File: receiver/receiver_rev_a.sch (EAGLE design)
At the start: 1 part

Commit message: Mostly done with the receiver
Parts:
- added C1, C2, C3: 100uF, microbuilder:CAP_CERAMIC1206
- added C4: 0.1uF, microbuilder:CAP_CERAMIC0603MINI
- added CN1: (no value), microbuilder:DCBARRELPTH
- added FID1, FID2, FID3, FID4, FID5, FID6: FIDUCIAL, adafruit:FIDUCIAL
- added FUSE: (no value), Custom:MINI-FUSE-HOLDER3557
- added J1: POWERPOLE_POWER45A_HORIZONTAL_DRILL, powerpoles:POWERPOLE_POWER45A_HORIZONTAL_DRILL
- added JP1: (no value), SparkFun-Connectors:M04PTH
- added JP2: (no value), SparkFun-Connectors:M02PTH4
- added OUT1, OUT2, OUT3: MC4, con-phoenix-381_l:MC4
- added Q1, Q2, Q3: (no value), Custom:DMN1019USN
- added R1, R10, R2, R3, R4, R5, R6, R7, R8, R9: 120, microbuilder:RESISTOR0603MINI
- added R11, R12: 220, microbuilder:RESISTOR0603MINI
- added R13, R14, R15: 10k, microbuilder:RESISTOR0603MINI
- added SWITCH: (no value), Custom:DIP-SWITCH-3PIN194
- added U$3, U$4, U$5, U$6: MOUNTINGHOLE2.5, microbuilder:MOUNTINGHOLE2.5
- added U$7: (no value), Custom:RJHSE-5381
- added U1: (no value), maxim:MAX3093/94UE
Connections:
- new net A+: R1.2, U$7.1, U1.A+
- new net A-: R1.1, U$7.2, U1.A-
- new net B+: R2.2, U$7.3, U1.B+
- new net B-: R2.1, U$7.6, U1.B-
- new net C+: R3.2, U$7.4, U1.C+
- new net C-: R3.1, U$7.5, U1.C-
- new net CLOCK: JP1.1, R6.2, R7.2, R9.2, U1.YD
- new net D+: R4.2, U$7.7, U1.D+
- new net D-: R4.1, U$7.8, U1.D-
- new net DATA1: JP1.4, R5.2, U1.YA
- new net DATA2: JP1.3, R8.2, U1.YB
- new net DATA3: JP1.2, R10.2, U1.YC
- new net GATE1: Q1.G, R13.1, SWITCH.1B
- new net GATE2: Q2.G, R14.1, SWITCH.2B
- new net GATE3: Q3.G, R15.1, SWITCH.3B
- new net GND: C4.P$2, CN1.GND, J1.GND, JP2.2, Q1.S, Q2.S, Q3.S, R11.1, R12.1, R13.2, R14.2, R15.2, U$7.SH, U1.GND
- new net N$1: OUT1.2.SK, R5.1
- new net N$10: R11.2, U$7.GC
- new net N$11: R12.2, U$7.YC
- new net N$2: OUT1.3.SK, R6.1
- new net N$3: C1.P$2, OUT1.4.SK, Q1.D
- new net N$4: OUT2.2.SK, R8.1
- new net N$5: OUT2.3.SK, R7.1
- new net N$6: C2.P$2, OUT2.4.SK, Q2.D
- new net N$7: OUT3.2.SK, R10.1
- new net N$8: OUT3.3.SK, R9.1
- new net N$9: C3.P$2, OUT3.4.SK, Q3.D
- new net PREFUSE_VCC: CN1.PWR, FUSE.1, J1.V+, JP2.1, U$7.YA
- new net VCC: C1.P$1, C2.P$1, C3.P$1, C4.P$1, FUSE.2, OUT1.1.SK, OUT2.1.SK, OUT3.1.SK, SWITCH.1A, SWITCH.2A, SWITCH.3A, U$7.GA, U1.ENAC, U1.ENBD, U1.VCC

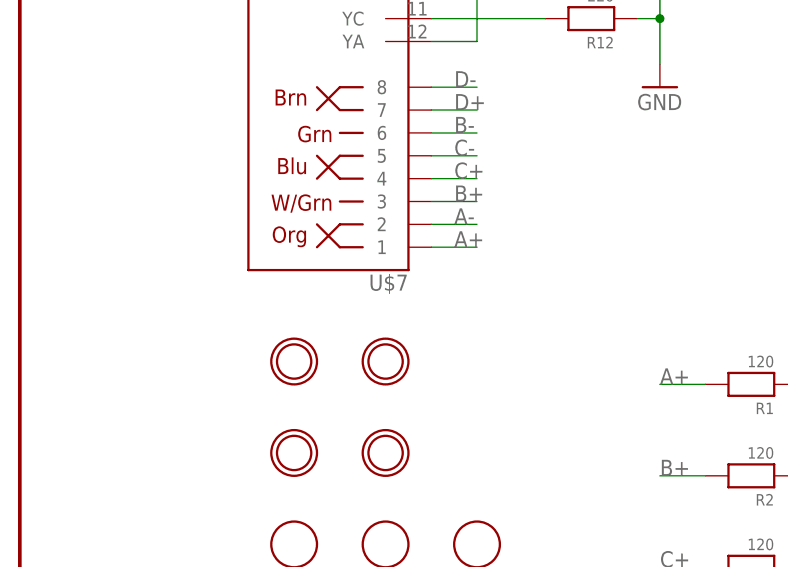
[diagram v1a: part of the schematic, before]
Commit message: Almost done with cape routing
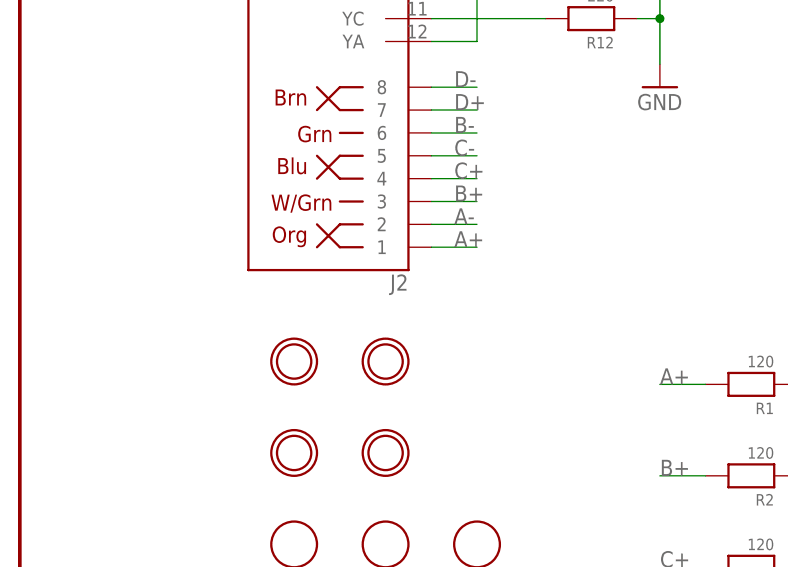
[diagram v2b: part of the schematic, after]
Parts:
- renumbered U$7 to J2
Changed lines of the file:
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@@
 <part name="U$5" library="microbuilder" deviceset="MOUNTINGHOLE" device="2.5"/>
 <part name="U$6" library="microbuilder" deviceset="MOUNTINGHOLE" device="2.5"/>
-<part name="U$7" library="Custom" deviceset="RJHSE-5381" device=""/>
+<part name="J2" library="Custom" deviceset="RJHSE-5381" device=""/>
 <part name="Q1" library="Custom" deviceset="DMN1019USN" device=""/>
 <part name="FUSE" library="Custom" deviceset="MINI-FUSE-HOLDER" device="3557"/>
@@
 <instance part="U$5" gate="G$1" x="40.64" y="58.42"/>
 <instance part="U$6" gate="G$1" x="30.48" y="48.26"/>
-<instance part="U$7" gate="G$1" x="33.02" y="81.28" rot="R180"/>
+<instance part="J2" gate="G$1" x="33.02" y="81.28" rot="R180"/>
 <instance part="Q1" gate="G$1" x="198.12" y="149.86"/>
 <instance part="FUSE" gate="G$1" x="63.5" y="154.94"/>
@@
 <net name="A+" class="0">
 <segment>
-<pinref part="U$7" gate="G$1" pin="1"/>
+<pinref part="J2" gate="G$1" pin="1"/>
 <wire x1="45.72" y1="71.12" x2="50.8" y2="71.12" width="0.1524" layer="91"/>
 <label x="48.26" y="71.12" size="1.778" layer="95"/>
@@
 <net name="A-" class="0">
 <segment>
-<pinref part="U$7" gate="G$1" pin="2"/>
+<pinref part="J2" gate="G$1" pin="2"/>
 <wire x1="45.72" y1="73.66" x2="50.8" y2="73.66" width="0.1524" layer="91"/>
 <label x="48.26" y="73.66" size="1.778" layer="95"/>
@@
 <net name="B+" class="0">
 <segment>
-<pinref part="U$7" gate="G$1" pin="3"/>
+<pinref part="J2" gate="G$1" pin="3"/>
 <wire x1="45.72" y1="76.2" x2="50.8" y2="76.2" width="0.1524" layer="91"/>
 <label x="48.26" y="76.2" size="1.778" layer="95"/>
@@
 <net name="C+" class="0">
 <segment>
-<pinref part="U$7" gate="G$1" pin="4"/>
+<pinref part="J2" gate="G$1" pin="4"/>
 <wire x1="45.72" y1="78.74" x2="50.8" y2="78.74" width="0.1524" layer="91"/>
 <label x="48.26" y="78.74" size="1.778" layer="95"/>
@@
 <net name="C-" class="0">
 <segment>
-<pinref part="U$7" gate="G$1" pin="5"/>
+<pinref part="J2" gate="G$1" pin="5"/>
 <wire x1="45.72" y1="81.28" x2="50.8" y2="81.28" width="0.1524" layer="91"/>
 <label x="48.26" y="81.28" size="1.778" layer="95"/>
@@
 <net name="B-" class="0">
 <segment>
-<pinref part="U$7" gate="G$1" pin="6"/>
+<pinref part="J2" gate="G$1" pin="6"/>
 <wire x1="45.72" y1="83.82" x2="50.8" y2="83.82" width="0.1524" layer="91"/>
 <label x="48.26" y="83.82" size="1.778" layer="95"/>
@@
 <net name="D+" class="0">
 <segment>
-<pinref part="U$7" gate="G$1" pin="7"/>
+<pinref part="J2" gate="G$1" pin="7"/>
 <wire x1="45.72" y1="86.36" x2="50.8" y2="86.36" width="0.1524" layer="91"/>
 <label x="48.26" y="86.36" size="1.778" layer="95"/>
@@
 <net name="D-" class="0">
 <segment>
-<pinref part="U$7" gate="G$1" pin="8"/>
+<pinref part="J2" gate="G$1" pin="8"/>
 <wire x1="45.72" y1="88.9" x2="50.8" y2="88.9" width="0.1524" layer="91"/>
 <label x="48.26" y="88.9" size="1.778" layer="95"/>
@@
 <segment>
 <pinref part="SUPPLY8" gate="G$1" pin="VCC"/>
-<pinref part="U$7" gate="G$1" pin="YA"/>
+<pinref part="J2" gate="G$1" pin="YA"/>
 <wire x1="50.8" y1="121.92" x2="50.8" y2="93.98" width="0.1524" layer="91"/>
 <wire x1="50.8" y1="93.98" x2="45.72" y2="93.98" width="0.1524" layer="91"/>
@@
 <segment>
 <pinref part="SUPPLY9" gate="G$1" pin="VCC"/>
-<pinref part="U$7" gate="G$1" pin="GA"/>
+<pinref part="J2" gate="G$1" pin="GA"/>
 <wire x1="55.88" y1="116.84" x2="55.88" y2="101.6" width="0.1524" layer="91"/>
 <wire x1="55.88" y1="101.6" x2="45.72" y2="101.6" width="0.1524" layer="91"/>
@@
 <wire x1="68.58" y1="96.52" x2="71.12" y2="96.52" width="0.1524" layer="91"/>
 <junction x="71.12" y="96.52"/>
-<pinref part="U$7" gate="G$1" pin="SH"/>
+<pinref part="J2" gate="G$1" pin="SH"/>
 <wire x1="45.72" y1="109.22" x2="71.12" y2="109.22" width="0.1524" layer="91"/>
 <wire x1="71.12" y1="109.22" x2="71.12" y2="104.14" width="0.1524" layer="91"/>
@@
 <net name="N$10" class="0">
 <segment>
-<pinref part="U$7" gate="G$1" pin="GC"/>
+<pinref part="J2" gate="G$1" pin="GC"/>
 <pinref part="R11" gate="G$1" pin="2"/>
 <wire x1="45.72" y1="104.14" x2="58.42" y2="104.14" width="0.1524" layer="91"/>
@@
 <net name="N$11" class="0">
 <segment>
-<pinref part="U$7" gate="G$1" pin="YC"/>
+<pinref part="J2" gate="G$1" pin="YC"/>
 <pinref part="R12" gate="G$1" pin="2"/>
 <wire x1="45.72" y1="96.52" x2="58.42" y2="96.52" width="0.1524" layer="91"/>
